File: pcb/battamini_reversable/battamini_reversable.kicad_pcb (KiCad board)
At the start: 2 copper layers, 128.3 x 99.3 mm, 38 parts

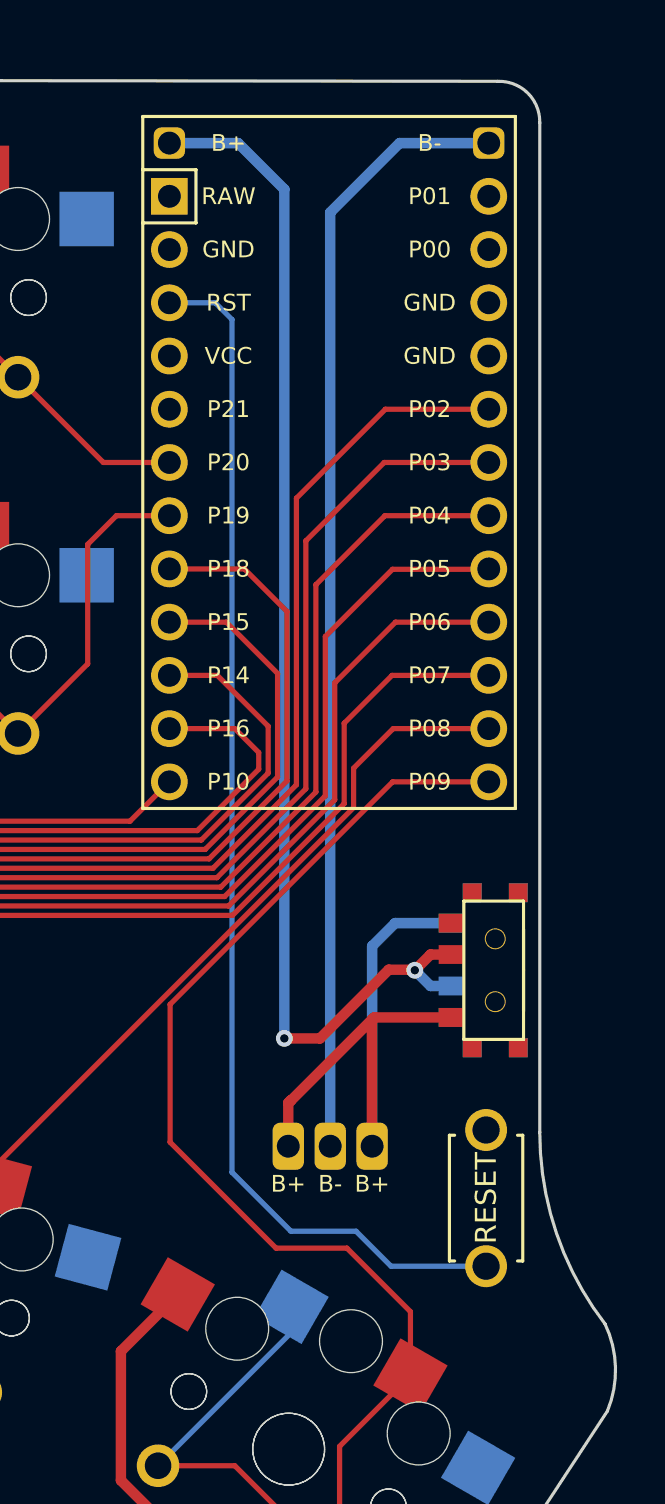
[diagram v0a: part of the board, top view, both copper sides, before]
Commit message: remove b- and b+
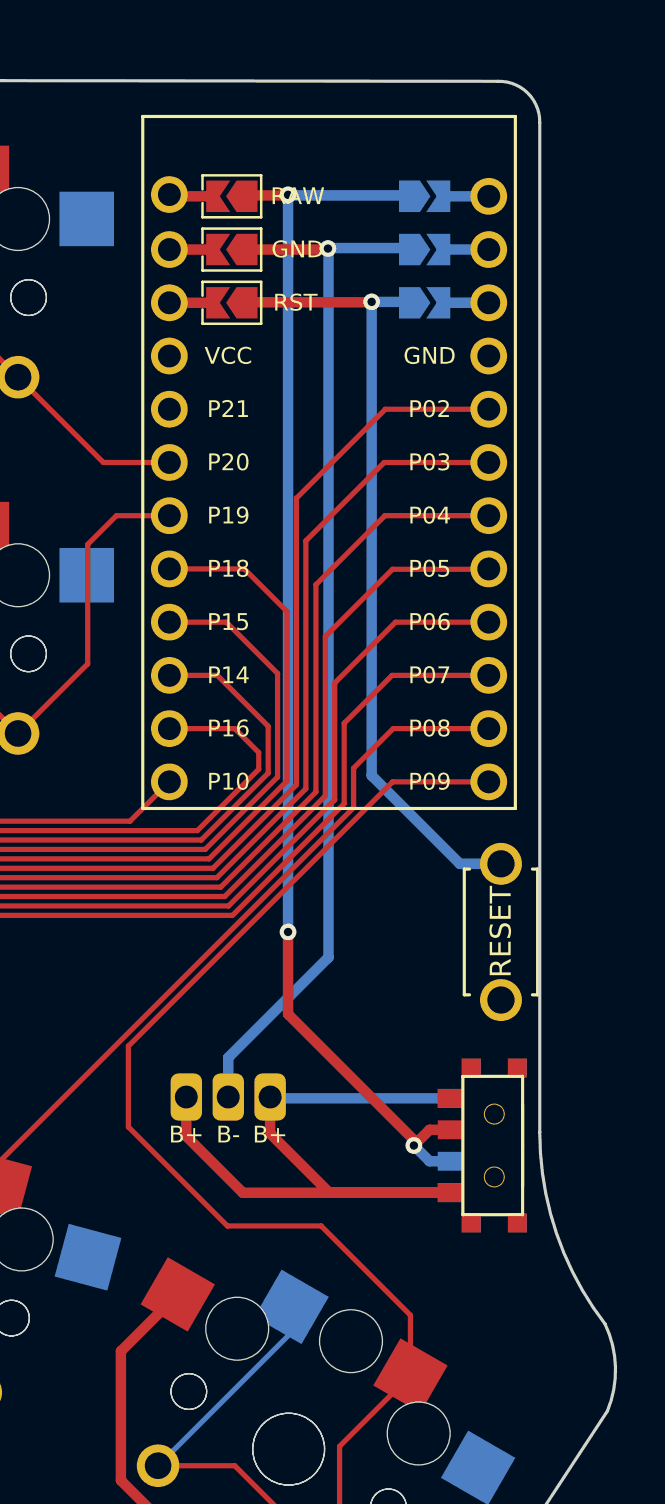
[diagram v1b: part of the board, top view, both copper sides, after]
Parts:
- moved B1 12.7 mm to (162.6, -66.0), turned to 90 degrees
- moved T1 8.36 mm to (162.2, -55.8)
- moved T2 8.36 mm to (162.2, -55.8)
- moved PAD1 5.40 mm to (149.5, -58.2)
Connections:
- MCU1 pad 2: GND -> Bgnd
- PAD1 pad 2: Bminus -> Bgnd
- T1 pad 2: Bplus -> RAW
- T2 pad 2: Bplus -> RAW
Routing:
- net RAW: track 0.00 -> 59.8 mm, vias 0 -> 3
- net Bplus: track 58.7 -> 0.00 mm, vias 2 -> 0
- net Bminus: track 53.5 -> 0.00 mm
- net Bgnd: track 0.00 -> 50.2 mm
- net RST: track 58.0 -> 38.3 mm, vias 0 -> 1
- net Braw: track 31.4 -> 35.8 mm
- net P9: track 75.7 -> 78.0 mm
- net GND: vias 0 -> 1

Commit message: rename the via
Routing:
- net GND: vias 1 -> 0
- net Bgnd: vias 0 -> 1
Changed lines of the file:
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@@
   (segment (start 126.242334 -75.958503) (end 126.242334 -83.060985) (width 0.5) (layer "F.Cu") (net 2))
   (segment (start 84.169651 -110.541422) (end 84.169651 -117.063993) (width 0.5) (layer "F.Cu") (net 2))
-  (via (at 154.304587 -98.650426) (size 0.8) (drill 0.4) (layers "F.Cu" "B.Cu") (free) (net 2))
   (segment (start 154.178854 -72.532303) (end 154.178854 -80.140845) (width 0.25) (layer "F.Cu") (net 3))
   (segment (start 157.383378 -83.345369) (end 161.96004 -83.345369) (width 0.25) (layer "F.Cu") (net 3))
@@
   (segment (start 154.256703 -98.602542) (end 150.44369 -98.602542) (width 0.5) (layer "F.Cu") (net 22))
   (segment (start 154.304587 -98.650426) (end 154.256703 -98.602542) (width 0.5) (layer "F.Cu") (net 22))
+  (via (at 154.304587 -98.650426) (size 0.8) (drill 0.4) (layers "F.Cu" "B.Cu") (free) (net 22))
   (segment (start 154.329345 -98.675184) (end 154.329345 -64.825511) (width 0.5) (layer "B.Cu") (net 22))
   (segment (start 149.545396 -60.041562) (end 149.545396 -58.163682) (width 0.5) (layer "B.Cu") (net 22))
